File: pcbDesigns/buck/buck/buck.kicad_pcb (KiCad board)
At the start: 2 copper layers, 85 x 105 mm, 17 parts, among them J1 GND, J2 5V, J3 ESP_CONNECTOR, J4 RECTIFIER_IN, J5 PWM_OUT, J6 CURR_SENS, Q1 IXGH24N60C4D1, U1 TLP250

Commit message: more revision
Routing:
- net VCC: track 47.9 -> 50.7 mm
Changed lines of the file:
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@@
   (segment (start 184 54) (end 180 50) (width 8) (layer "F.Cu") (net 3))
   (segment (start 169.75 47.5) (end 180 47.5) (width 6.5) (layer "B.Cu") (net 3))
-  (segment (start 200.5 64.9) (end 175.65 64.9) (width 8.5) (layer "B.Cu") (net 4))
   (segment (start 187.5 47.5) (end 187.5 51.25) (width 8) (layer "B.Cu") (net 4))
   (segment (start 187.5 51.25) (end 174.75 64) (width 8) (layer "B.Cu") (net 4))
-  (segment (start 175.65 64.9) (end 174.75 64) (width 10) (layer "B.Cu") (net 4))
+  (segment (start 200.5 64.9) (end 177.65 64.9) (width 8.5) (layer "B.Cu") (net 4))
+  (segment (start 174.75 62) (end 174.75 64) (width 10) (layer "B.Cu") (net 4))
+  (segment (start 177.65 64.9) (end 174.75 62) (width 8.5) (layer "B.Cu") (net 4))
   (segment (start 187.0885 116.0885) (end 190.8085 119.8085) (width 2) (layer "F.Cu") (net 5))
   (segment (start 187.0885 112.6085) (end 187.0885 116.0885) (width 2) (layer "F.Cu") (net 5))
@@
     (polygon
       (pts
-        (xy 168.5 70)
+        (xy 167.5 70)
         (xy 158 70)
         (xy 158 57.5)
-        (xy 168.5 57.5)
+        (xy 167.5 57.5)
       )
     )

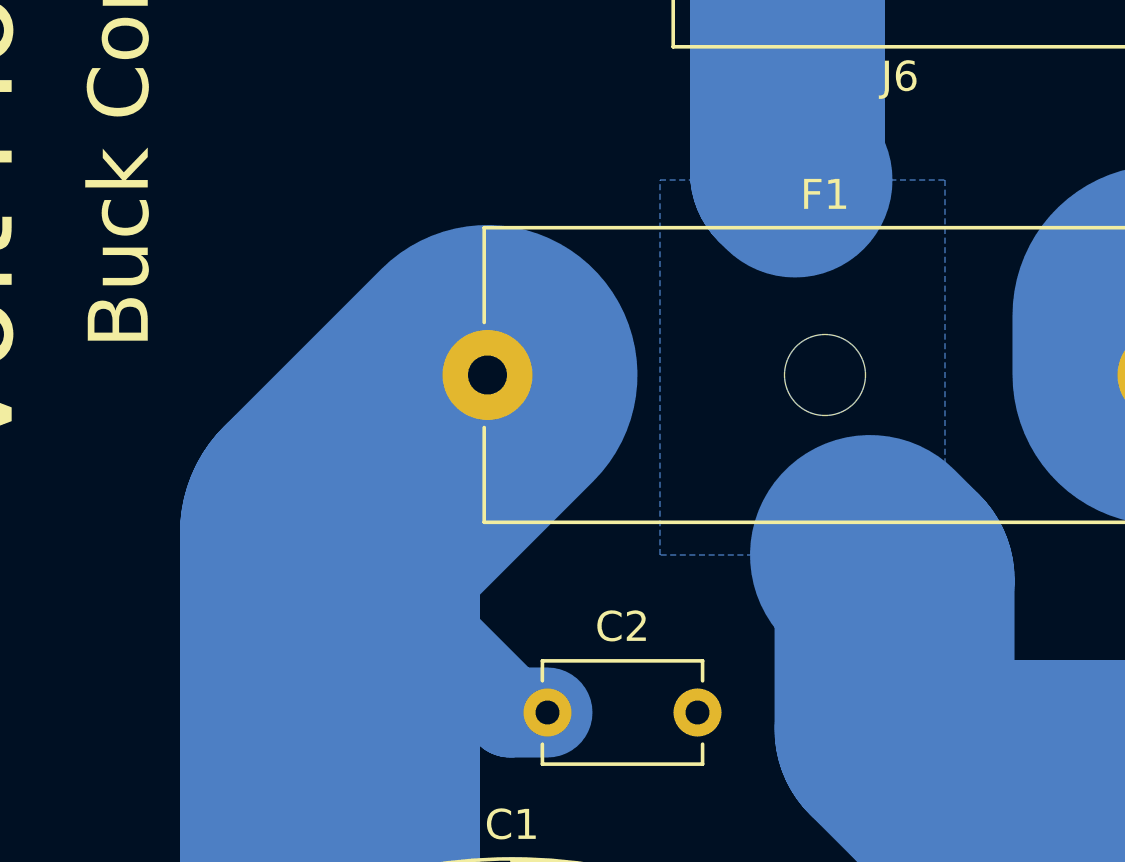
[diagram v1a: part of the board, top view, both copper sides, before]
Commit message: revision: buck pcb design
increase clearance
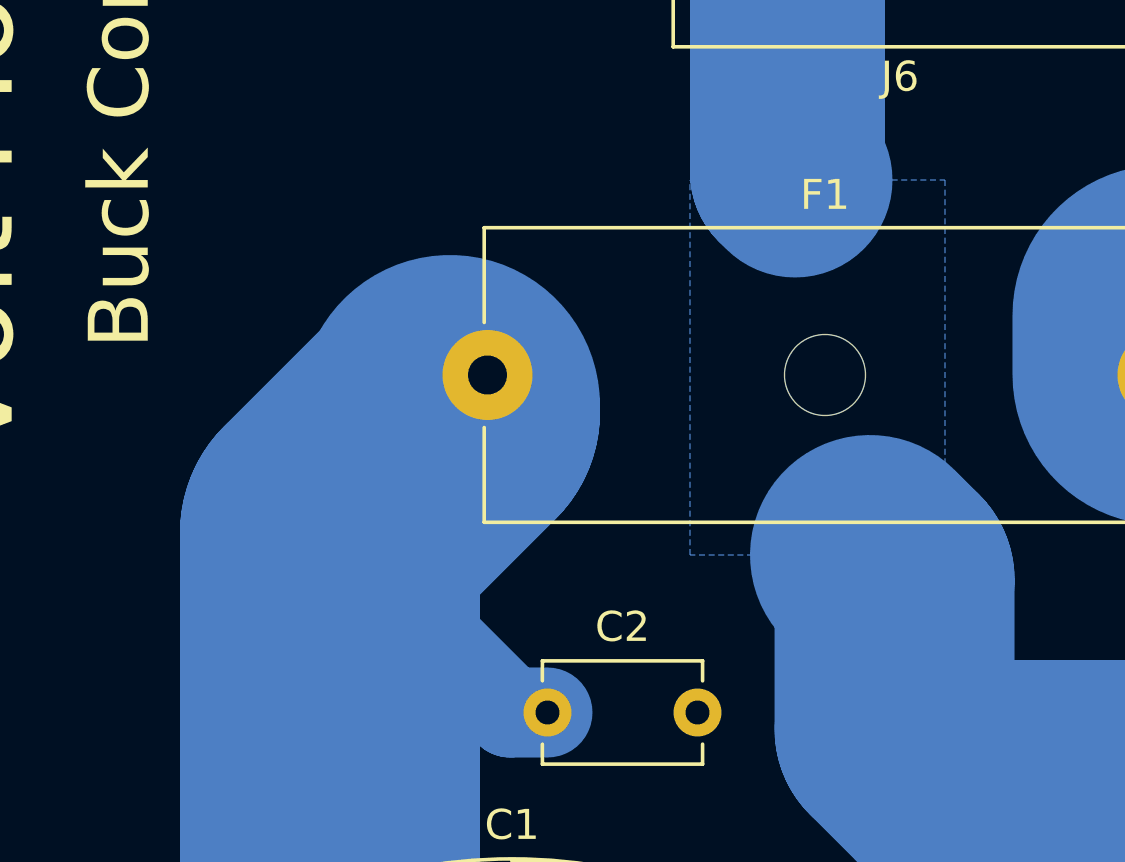
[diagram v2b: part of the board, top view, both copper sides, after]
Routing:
- net Net-(C1-Pad1): track 74.7 -> 73.1 mm
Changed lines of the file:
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@@
     (effects (font (size 2 2) (thickness 0.15)))
   )
+  (segment (start 147 69.25) (end 151 65.25) (width 10) (layer "B.Cu") (net 1))
   (segment (start 147 126.75) (end 147 69.25) (width 10) (layer "B.Cu") (net 1))
+  (segment (start 151 65.25) (end 151 65) (width 10) (layer "B.Cu") (net 1))
   (segment (start 153 75.25) (end 147 69.25) (width 3) (layer "B.Cu") (net 1))
   (segment (start 154.25 75.25) (end 153 75.25) (width 3) (layer "B.Cu") (net 1))
-  (segment (start 147 69.25) (end 152.25 64) (width 10) (layer "B.Cu") (net 1))
   (segment (start 177.51913 106.3615) (end 178.145641 106.988011) (width 2) (layer "B.Cu") (net 2))
   (segment (start 188.378989 106.988011) (end 189.6285 105.7385) (width 2) (layer "B.Cu") (net 2))
@@
   (segment (start 187.0885 104.9885) (end 187.0885 102.3985) (width 2) (layer "F.Cu") (net 12))
   (zone (net 2) (net_name "GNDPWR") (layer "F.Cu") (hatch edge 0.508)
-    (connect_pads yes (clearance 0))
+    (connect_pads yes (clearance 2))
     (min_thickness 0.254) (filled_areas_thickness no)
     (fill yes (thermal_gap 0.508) (thermal_bridge_width 0.508))
@@
       (pts
         (xy 167.5 70)
-        (xy 158 70)
-        (xy 158 57.5)
+        (xy 159 70)
+        (xy 159 57.5)
         (xy 167.5 57.5)
       )
